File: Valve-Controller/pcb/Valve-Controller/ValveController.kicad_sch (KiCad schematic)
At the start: 8 parts, among them Q1 SiS454DN

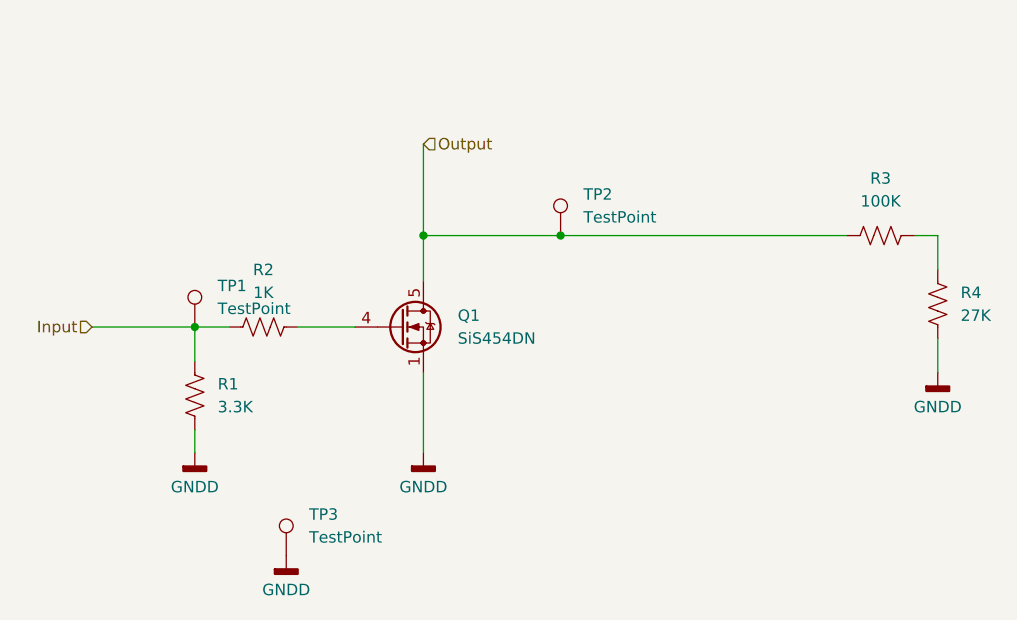
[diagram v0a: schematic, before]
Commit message: Valve controller diode
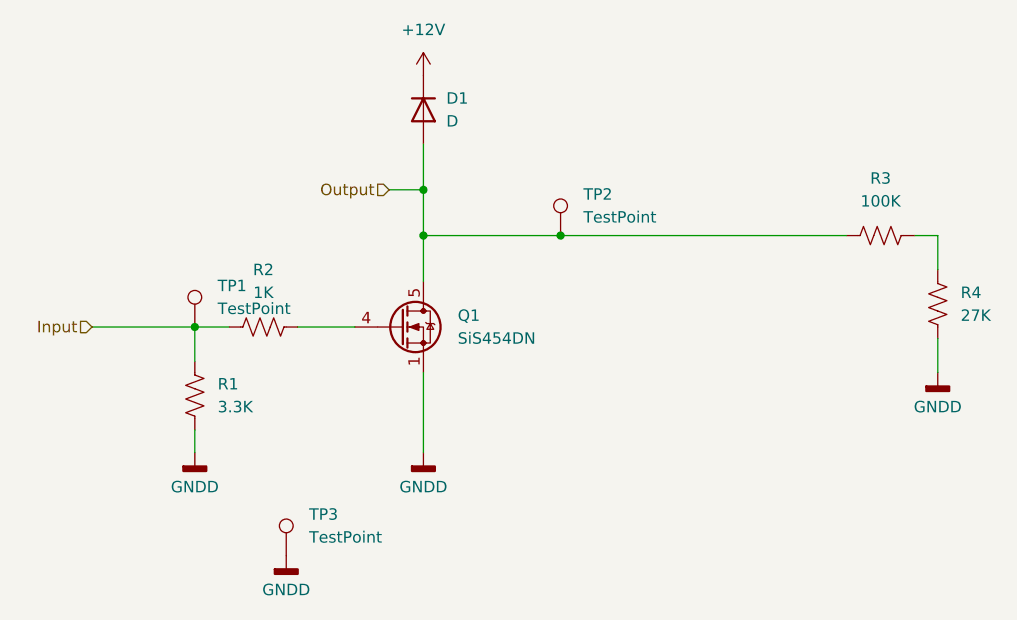
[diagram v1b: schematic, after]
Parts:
- added D1: D, Diode_SMD:D_SOD-123, symbol Device:D
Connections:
- net Output: now also D1.2 (A)
- new net +12V: D1.1 (K)
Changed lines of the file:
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@@
+	)
+	(junction
+		(at 115.57 72.39)
+		(diameter 0)
+		(color 0 0 0 0)
 	)
 	(junction
@@
 	(wire
 		(pts
-			(xy 115.57 67.31) (xy 115.57 77.47)
+			(xy 111.76 72.39) (xy 115.57 72.39)
+		)
+		(stroke
+			(width 0)
+			(type default)
+		)
+	)
+	(wire
+		(pts
+			(xy 115.57 67.31) (xy 115.57 72.39)
 		)
 		(stroke
@@
 		(pts
 			(xy 172.72 77.47) (xy 172.72 81.28)
+		)
+		(stroke
+			(width 0)
+			(type default)
+		)
+	)
+	(wire
+		(pts
+			(xy 115.57 72.39) (xy 115.57 77.47)
 		)
 		(stroke
@@
 	(hierarchical_label "Output"
 		(shape input)
-		(at 115.57 67.31 0)
+		(at 111.76 72.39 180)
 		(fields_autoplaced yes)
 		(effects
@@
 				(size 1.27 1.27)
 			)
-			(justify left)
+			(justify right)
 		)
 	)
@@
 	)
 	(symbol
+		(lib_id "Device:D")
+		(at 115.57 63.5 270)
+		(unit 1)
+		(exclude_from_sim no)
+		(in_bom yes)
+		(on_board yes)
+		(dnp no)
+		(fields_autoplaced yes)
+		(property "Reference" "D1"
+			(at 118.11 62.2299 90)
+			(effects
+				(font
+					(size 1.27 1.27)
+				)
+				(justify left)
+			)
+		)
+		(property "Value" "D"
+			(at 118.11 64.7699 90)
+			(effects
+				(font
+					(size 1.27 1.27)
+				)
+				(justify left)
+			)
+		)
+		(property "Footprint" "Diode_SMD:D_SOD-123"
+			(at 115.57 63.5 0)
+			(effects
+				(font
+					(size 1.27 1.27)
+				)
+				(hide yes)
+			)
+		)
+		(property "Datasheet" "~"
+			(at 115.57 63.5 0)
+			(effects
+				(font
+					(size 1.27 1.27)
+				)
+				(hide yes)
+			)
+		)
+		(property "Description" "Diode"
+			(at 115.57 63.5 0)
+			(effects
+				(font
+					(size 1.27 1.27)
+				)
+				(hide yes)
+			)
+		)
+		(property "Sim.Device" "D"
+			(at 115.57 63.5 0)
+			(effects
+				(font
+					(size 1.27 1.27)
+				)
+				(hide yes)
+			)
+		)
+		(property "Sim.Pins" "1=K 2=A"
+			(at 115.57 63.5 0)
+			(effects
+				(font
+					(size 1.27 1.27)
+				)
+				(hide yes)
+			)
+		)
+		(pin "1"
+		)
+		(pin "2"
+		)
+		(instances
+			(project ""
+				(path "/3d6591d1-15d3-4f90-b463-ad4ce370627d/d3fae8d6-dc5c-4ad1-8056-ef8170011280"
+					(reference "D1")
+					(unit 1)
+				)
+			)
+		)
+	)
+	(symbol
 		(lib_id "power:GNDD")
 		(at 172.72 92.71 0)
@@
 					(unit 1)
 				)
+			)
+		)
+	)
+	(symbol
+		(lib_id "power:+12V")
+		(at 115.57 59.69 0)
+		(unit 1)
+		(exclude_from_sim no)
+		(in_bom yes)
+		(on_board yes)
+		(dnp no)
+		(fields_autoplaced yes)
+		(property "Reference" "#PWR08"
+			(at 115.57 63.5 0)
+			(effects
+				(font
+					(size 1.27 1.27)
+				)
+				(hide yes)
+			)
+		)
+		(property "Value" "+12V"
+			(at 115.57 54.61 0)
+			(effects
+				(font
+					(size 1.27 1.27)
+				)
+			)
+		)
+		(property "Footprint" ""
+			(at 115.57 59.69 0)
+			(effects
+				(font
+					(size 1.27 1.27)
+				)
+				(hide yes)
+			)
+		)
+		(property "Datasheet" ""
+			(at 115.57 59.69 0)
+			(effects
+				(font
+					(size 1.27 1.27)
+				)
+				(hide yes)
+			)
+		)
+		(property "Description" "Power symbol creates a global label with name \"+12V\""
+			(at 115.57 59.69 0)
+			(effects
+				(font
+					(size 1.27 1.27)
+				)
+				(hide yes)
+			)
+		)
+		(pin "1"
+		)
+		(instances
+			(project ""
+				(path "/3d6591d1-15d3-4f90-b463-ad4ce370627d/d3fae8d6-dc5c-4ad1-8056-ef8170011280"
+					(reference "#PWR08")
+					(unit 1)
+				)

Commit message: Updated Valve Controller PCB and BOM
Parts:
- D1: Purchase (none) -> https://www.digikey.com/en/products/detail/onsemi/MMSD4148T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
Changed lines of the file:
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@@
 			)
 		)
-		(property "Datasheet" "~"
+		(property "Datasheet" "https://www.onsemi.com/pdf/datasheet/mmsd4148t1-d.pdf"
 			(at 115.57 63.5 0)
 			(effects
@@
 			(at 115.57 63.5 0)
 			(effects
+				(font
+					(size 1.27 1.27)
+				)
+				(hide yes)
+			)
+		)
+		(property "Purchase" "https://www.digikey.com/en/products/detail/onsemi/MMSD4148T1G/919705"
+			(at 115.57 63.5 0)
+			(effects
